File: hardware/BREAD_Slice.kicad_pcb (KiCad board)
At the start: 2 copper layers, 70 x 100 mm, 22 parts, among them J1 Conn_01x10_Socket, SW1 SW_DIP_x04, U1 AP63205

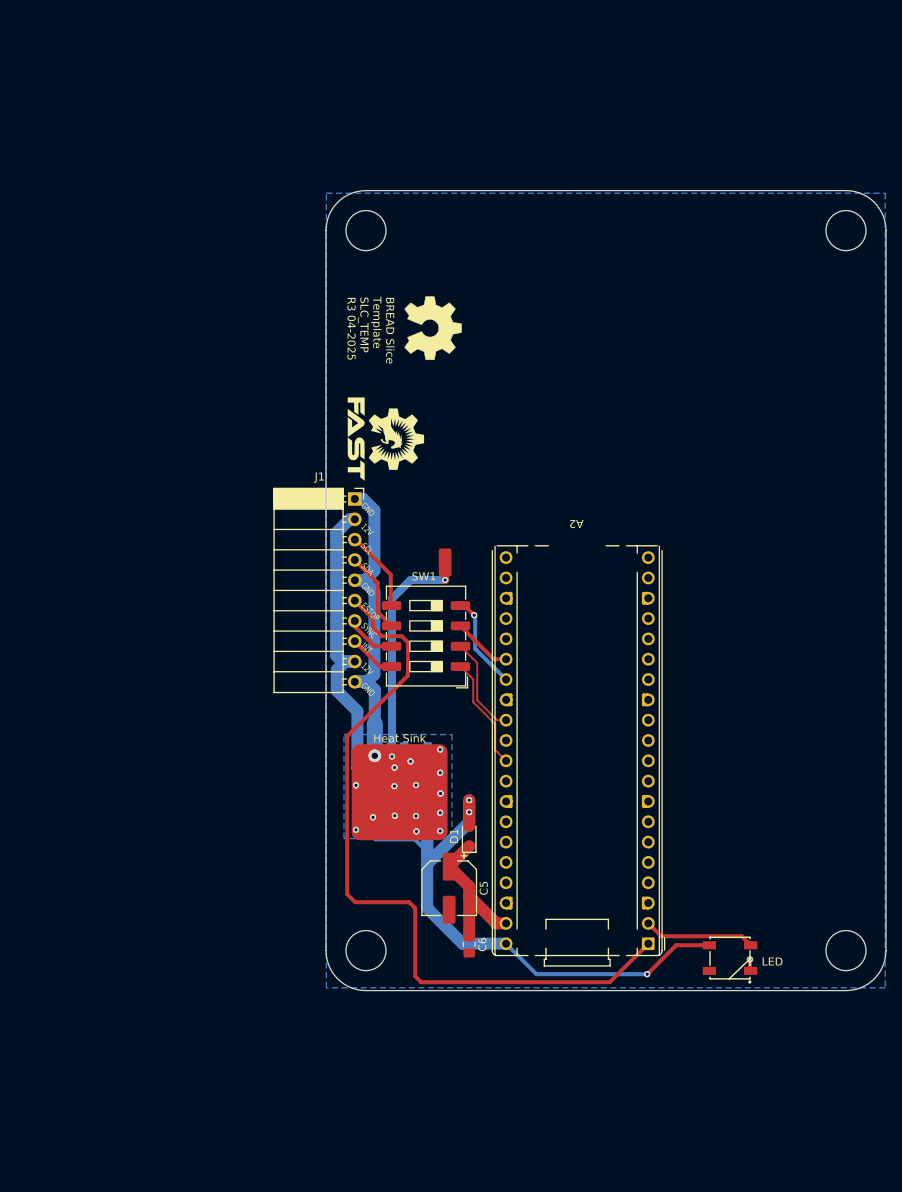
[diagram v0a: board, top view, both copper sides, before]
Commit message: changed dimensions to match 100x145mm standard for large format
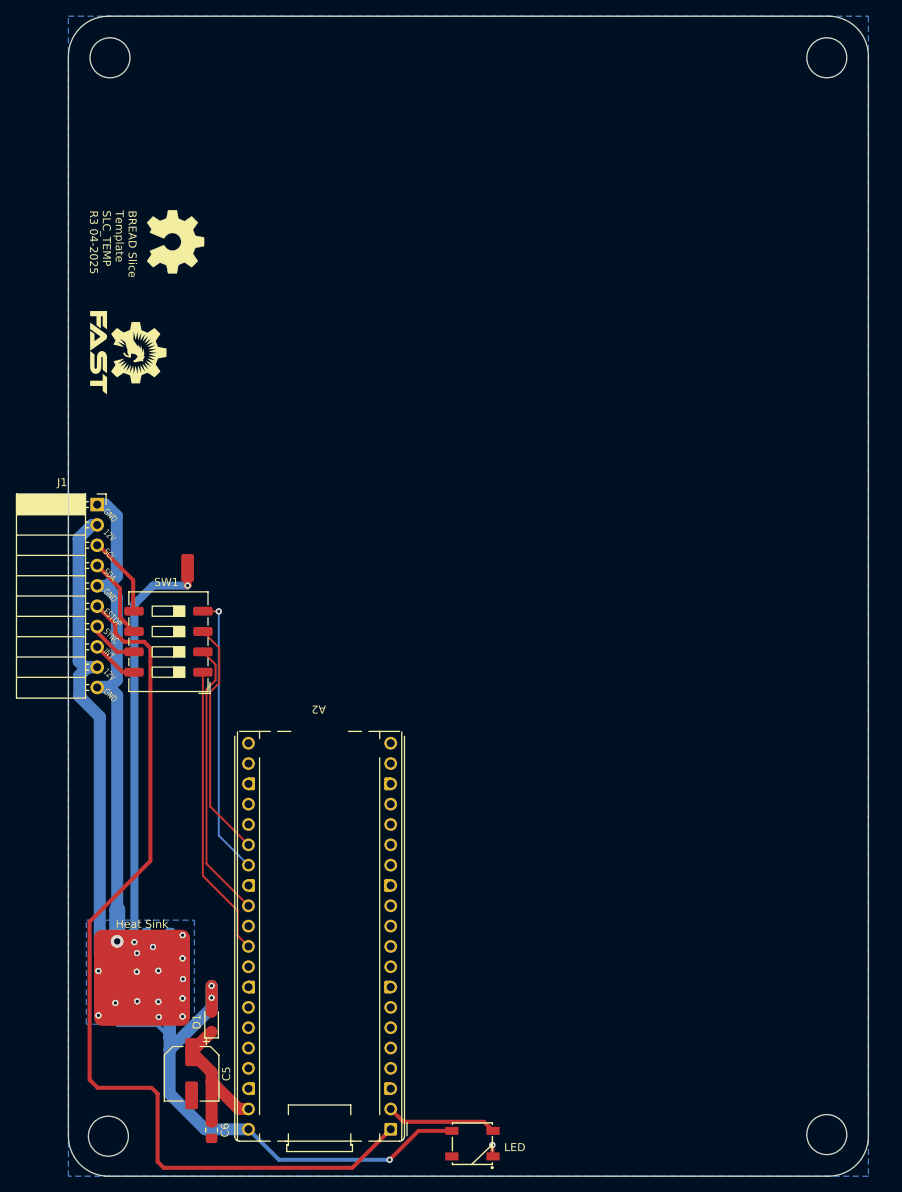
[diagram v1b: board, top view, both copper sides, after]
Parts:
- moved C6 39.7 mm to (108.3, 157.2)
- moved C1 39.7 mm to (96.6, 135.9)
- moved HS1 39.7 mm to (99.6, 138.2)
- moved D2 39.7 mm to (140.9, 158.9)
- moved NT1 39.7 mm to (96.5, 131.6)
- moved C2 39.7 mm to (99.0, 142.7)
- moved C3 39.7 mm to (101.7, 135.9)
- moved C4 39.7 mm to (101.7, 132.8)
- moved C5 39.7 mm to (105.8, 150.2)
- moved D1 39.7 mm to (108.3, 143.7)
- moved U1 39.7 mm to (96.5, 139.2)
- moved A2 39.7 mm to (130.7, 157.1)
- moved H2 39.7 mm to (95.4, 158.0)
- moved L1 39.7 mm to (101.7, 139.2)
- moved H1 38.6 mm to (95.6, 23.2)
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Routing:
- net /slice_template/I2C0_CLK/GPIO21: track 11.9 -> 35.3 mm
- net /slice_template/SYNC/CAN_{INT}: track 12.3 -> 35.0 mm
- net /slice_template/I2C0_SDA/GPIO20: track 7.42 -> 30.0 mm
- net GNDPWR: track 36.9 -> 59.4 mm
- net GND: track 47.6 -> 70.1 mm
- net /slice_template/ESTOP: track 93.9 -> 116.4 mm
- net +12V: track 41.4 -> 63.9 mm
- net /slice_template/INT/CAN_{CS}: track 14.1 -> 36.6 mm
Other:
- board size 70 x 100 mm -> 100 x 145 mm

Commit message: added inner layers
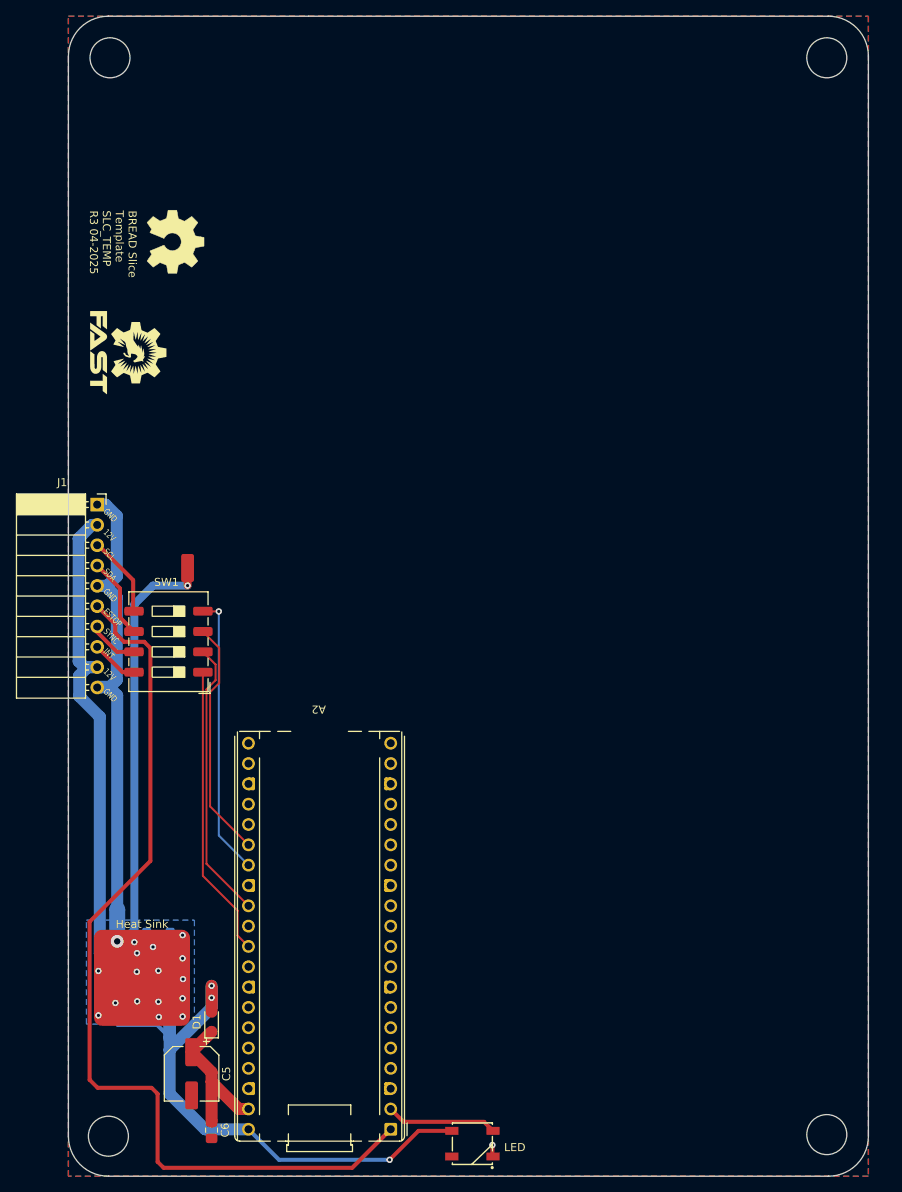
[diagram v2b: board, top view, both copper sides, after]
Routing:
- added copper zone on F.Cu, net GND
- added copper zone on In1.Cu, net GND
- added copper zone on In2.Cu, net GND
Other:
- copper layers 2 -> 4
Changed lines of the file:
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@@
 	(layers
 		(0 "F.Cu" signal)
+		(4 "In1.Cu" signal)
+		(6 "In2.Cu" signal)
 		(2 "B.Cu" signal)
 		(9 "F.Adhes" user "F.Adhesive")
@@
 			)
 			(layer "dielectric 1"
+				(type "prepreg")
+				(thickness 0.1)
+				(material "FR4")
+				(epsilon_r 4.5)
+				(loss_tangent 0.02)
+			)
+			(layer "In1.Cu"
+				(type "copper")
+				(thickness 0.035)
+			)
+			(layer "dielectric 2"
 				(type "core")
-				(thickness 1.51)
+				(thickness 1.24)
+				(material "FR4")
+				(epsilon_r 4.5)
+				(loss_tangent 0.02)
+			)
+			(layer "In2.Cu"
+				(type "copper")
+				(thickness 0.035)
+			)
+			(layer "dielectric 3"
+				(type "prepreg")
+				(thickness 0.1)
 				(material "FR4")
 				(epsilon_r 4.5)
@@
 		(net 3)
 		(net_name "GND")
-		(layer "B.Cu")
-		(hatch edge 0.5)
-		(priority 1)
+		(layers "F.Cu" "B.Cu" "In1.Cu" "In2.Cu")
+		(hatch edge 0.508)
 		(connect_pads
-			(clearance 0.4)
+			(clearance 0.5)
 		)
 		(min_thickness 0.25)
 		(filled_areas_thickness no)
 		(fill yes
-			(thermal_gap 0.3)
-			(thermal_bridge_width 3)
+			(thermal_gap 0.5)
+			(thermal_bridge_width 0.5)
 		)
 		(polygon
 			(pts
-				(xy 92.65 130.995) (xy 106.15 130.995) (xy 106.15 143.995) (xy 92.65 143.995)
+				(xy 190.4 163) (xy 90.4 163) (xy 90.4 18) (xy 190.4 18)
 			)
 		)
@@
 		(net_name "GND")
 		(layer "B.Cu")
-		(hatch edge 0.508)
+		(hatch edge 0.5)
+		(priority 1)
 		(connect_pads
-			(clearance 0.5)
+			(clearance 0.4)
 		)
 		(min_thickness 0.25)
 		(filled_areas_thickness no)
 		(fill yes
-			(thermal_gap 0.5)
-			(thermal_bridge_width 0.5)
+			(thermal_gap 0.3)
+			(thermal_bridge_width 3)
 		)
 		(polygon
 			(pts
-				(xy 190.4 163) (xy 90.4 163) (xy 90.4 18) (xy 190.4 18)
+				(xy 92.65 130.995) (xy 106.15 130.995) (xy 106.15 143.995) (xy 92.65 143.995)
 			)
 		)

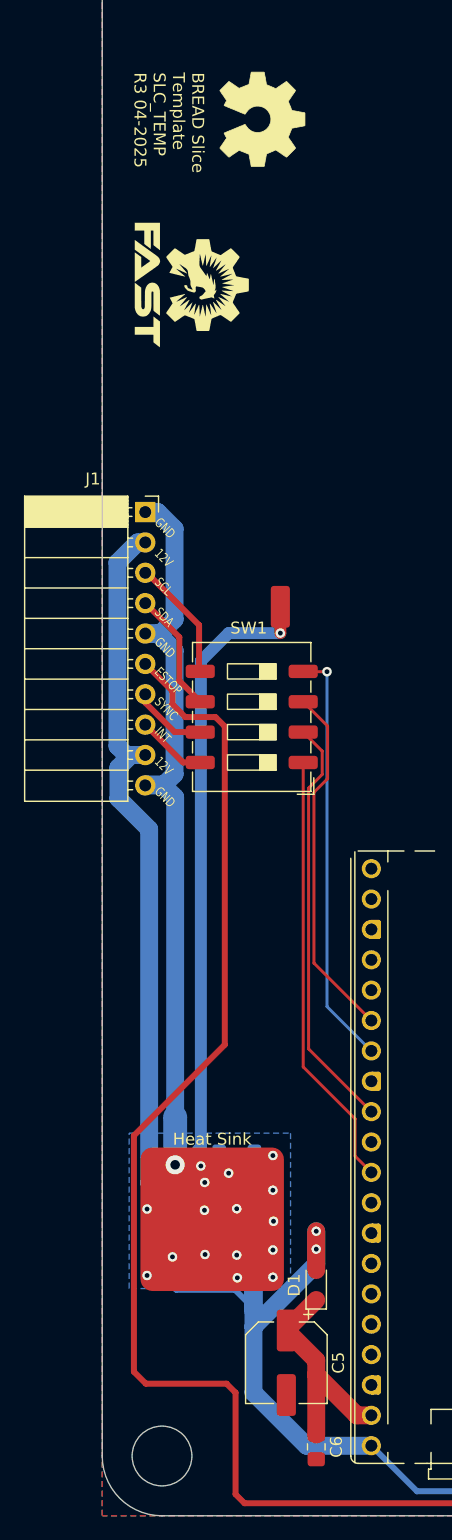
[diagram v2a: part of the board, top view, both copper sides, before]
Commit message: pcb: change backplane connector to be consistent offset from bottom edge and reroute
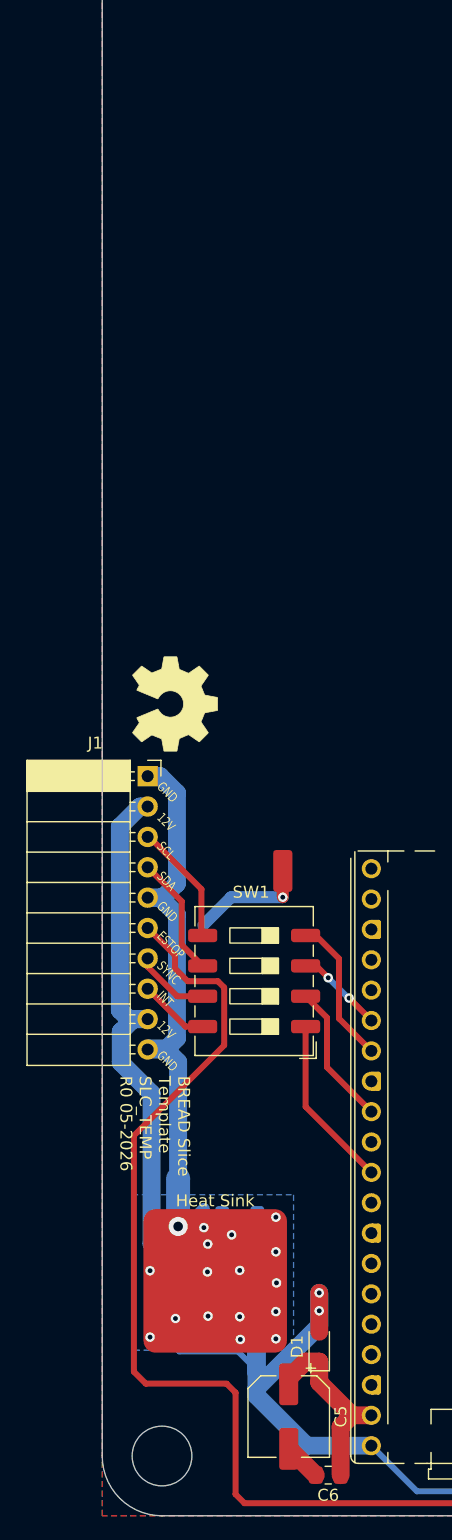
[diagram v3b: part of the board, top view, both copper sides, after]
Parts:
- removed G***: LOGO, KMLib_Aesthetic:FAST-Logo-Medium
- moved Ref** 49.4 mm to (96.1, 95.1)
- moved ? 22.1 mm to (105.5, 109.1)
- moved J1 22.1 mm to (94.2, 101.1)
- moved SW1 22.1 mm to (103.1, 118.3)
- moved C1 5.16 mm to (96.8, 141.1)
- moved C2 5.16 mm to (99.2, 147.9)
- moved C3 5.16 mm to (101.9, 141.1)
- moved C4 5.16 mm to (101.9, 138.0)
- moved D1 5.16 mm to (108.5, 148.9)
- moved HS1 5.16 mm to (99.8, 143.4)
- moved L1 5.16 mm to (101.9, 144.4)
- moved NT1 5.16 mm to (96.8, 136.8)
- moved U1 5.16 mm to (96.8, 144.4)
- moved C5 4.50 mm to (106.0, 154.7)
- moved C6 2.57 mm to (109.3, 159.6), turned to 180 degrees
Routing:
- net GND: track 70.1 -> 32.6 mm
- net /slice_template/SYNC/CAN_{INT}: track 35.0 -> 11.9 mm
- net /slice_template/I2C0_CLK/GPIO21: track 35.3 -> 12.5 mm, vias 1 -> 0
- net /slice_template/I2C0_SDA/GPIO20: track 30.0 -> 7.41 mm, vias 0 -> 2
- net /slice_template/ESTOP: track 116.4 -> 94.1 mm
- net /slice_template/INT/CAN_{CS}: track 36.6 -> 14.5 mm
- net GNDPWR: track 59.4 -> 42.5 mm
- net +12V: track 63.9 -> 47.0 mm
- net +5V: track 87.3 -> 82.1 mm
- net /slice_template/VSYS: track 19.3 -> 16.3 mm
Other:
- board text added: "BREAD Slice Template SLC_TEMP R0 05-2026"
- board text removed: "BREAD Slice Template SLC_TEMP R3 04-2025"

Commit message: chore: change version to v1 to align with template name
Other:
- board text added: "BREAD Slice Template SLC_TEMP R1 05-2026"
- board text removed: "BREAD Slice Template SLC_TEMP R0 05-2026"
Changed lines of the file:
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@@
 		)
 	)
-	(gr_text "BREAD Slice\nTemplate\nSLC_TEMP\nR0 05-2026"
+	(gr_text "BREAD Slice\nTemplate\nSLC_TEMP\nR1 05-2026"
 		(at 94.8 126.2 270)
 		(layer "F.SilkS")

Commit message: fix: clear erc/drc errors
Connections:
- net /slice_template/AGND renamed GNDA
- A2 pad 4: unconnected-(A2-GPIO2-Pad4) -> /slice_template/GPIO2
- A2 pad 5: unconnected-(A2-GPIO3-Pad5) -> /slice_template/GPIO3
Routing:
- net GND: track 32.6 -> 41.1 mm
